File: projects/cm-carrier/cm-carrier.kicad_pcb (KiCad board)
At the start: 4 copper layers, 130 x 90 mm, 93 parts, among them J1 XA_5V_IN, J2 DEBUG_UART, J3 USB_C_HOST (USB2.0), J4 XA_USB1, J5 XA_USB2, J6 EC25-J Mini PCIe, J7 nanoSIM, J8 micro HDMI (Type D), J9 microSD, Q1 2N7002, Q2 2N7002, SW1 PWR_BUT, U1 TPS62132, U10 TPD4EUSB30, U11 TPD4EUSB30, U12 MagJack A70-112-331N126, U13 TPD4EUSB30, U14 TPD4EUSB30, U15 TPD4EUSB30, U16 RT9742SNGV, U17 RT9742GGJ5, U2 USB2514B-I/M2, U3 TPS2051CDBV, U4 TPS2051CDBV, U5 TPS2051CDBV, U6 USBLC6-2SC6, U7 USBLC6-2SC6, U8 USBLC6-2SC6, U9 TPD4E05U06DQA, Y1 24MHz CL=18pF

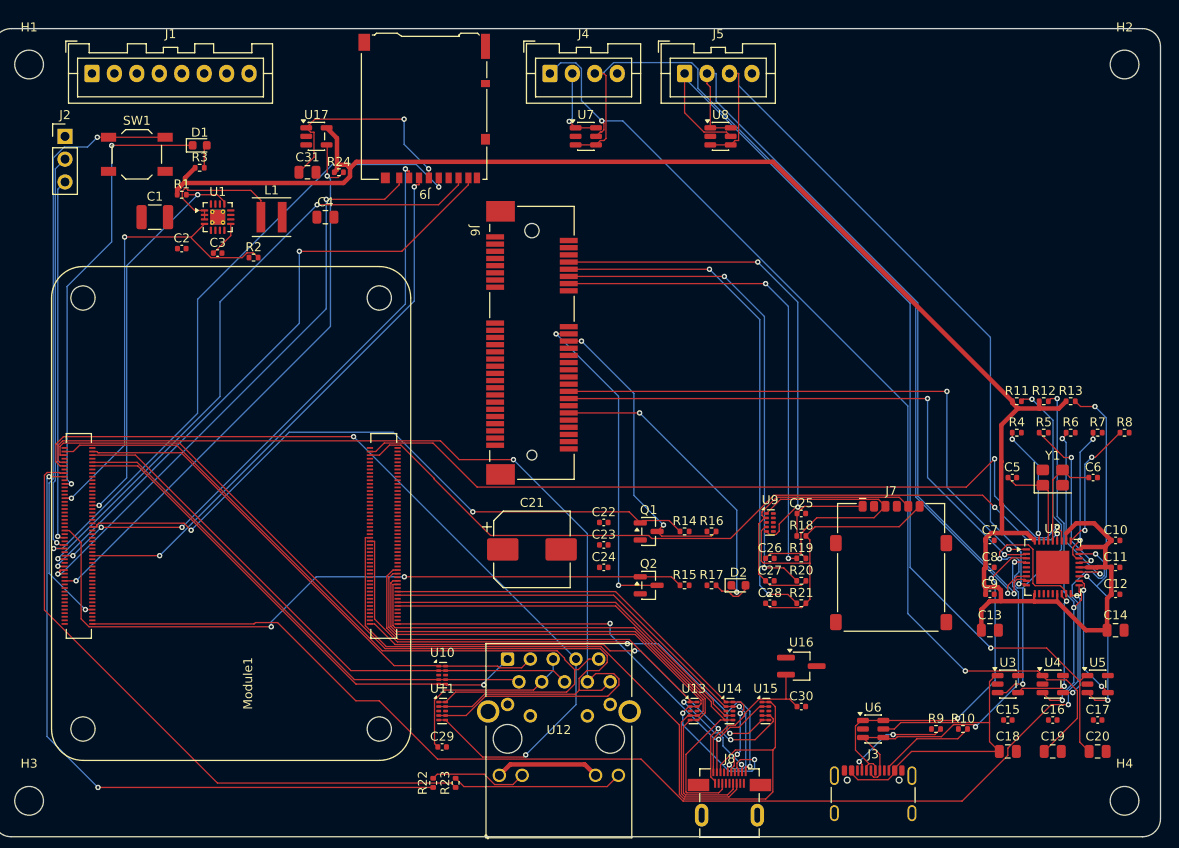
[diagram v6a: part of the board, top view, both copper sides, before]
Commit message: cm-carrier: 166 plane-connection vias with stubs (planned by script, placed via Konnect add_via/route_trace)
Co-Authored-By: Claude Opus 5.5 <noreply@anthropic.com>
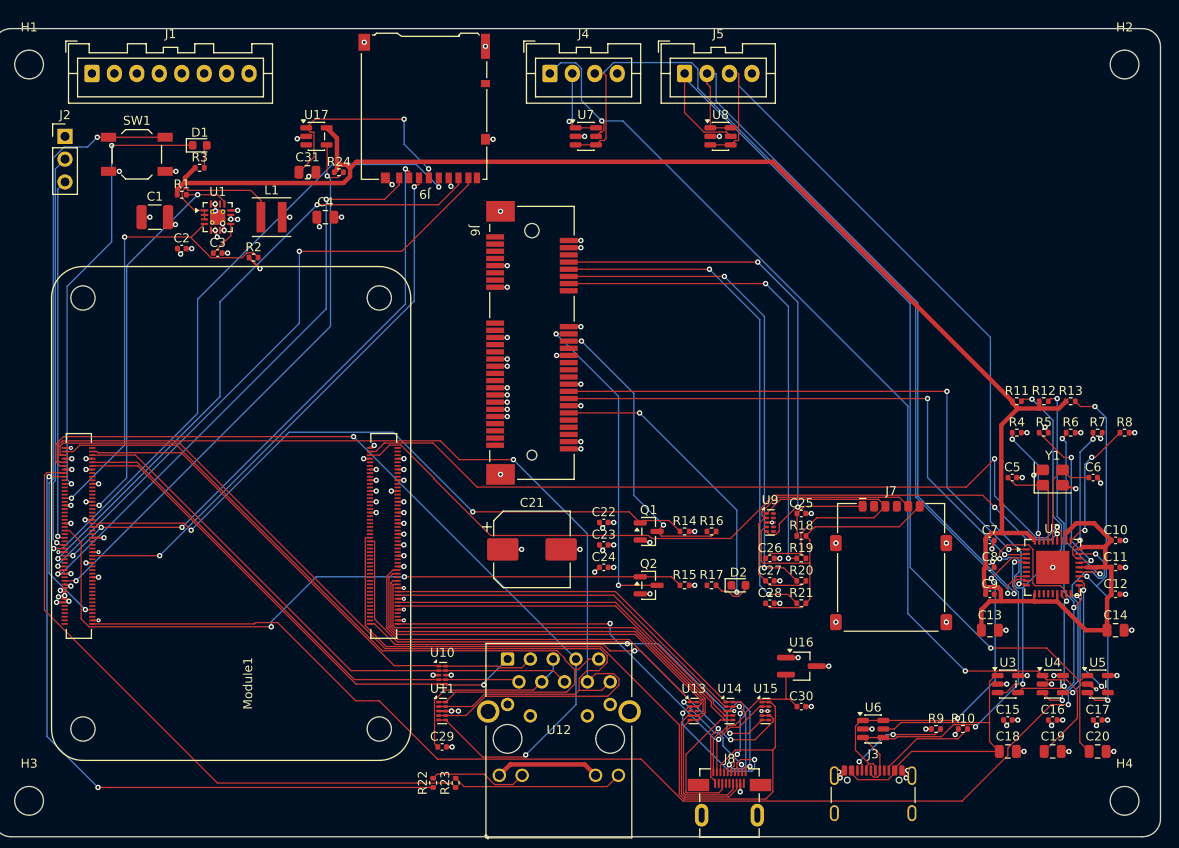
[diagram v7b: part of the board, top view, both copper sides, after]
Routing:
- net GND: track 0.00 -> 108.2 mm, vias 0 -> 135
- net +5V: track 0.00 -> 15.4 mm, vias 0 -> 20
- net +3V3_LTE: track 0.00 -> 13.3 mm, vias 0 -> 11
